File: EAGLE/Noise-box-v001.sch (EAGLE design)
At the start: 83 parts, among them J1 AVR_SPI_PROG_3X22X3_LOCK, J4 MICRO-SD_CARD_SOCKET, J5 HEADPHONE, J6 POWER_JACK, U1 ATMEGA328P_TQFP, U2 MIC5219 3.3V, U3 MCP73831, Y1 12.288MHz, Y2 8MHz

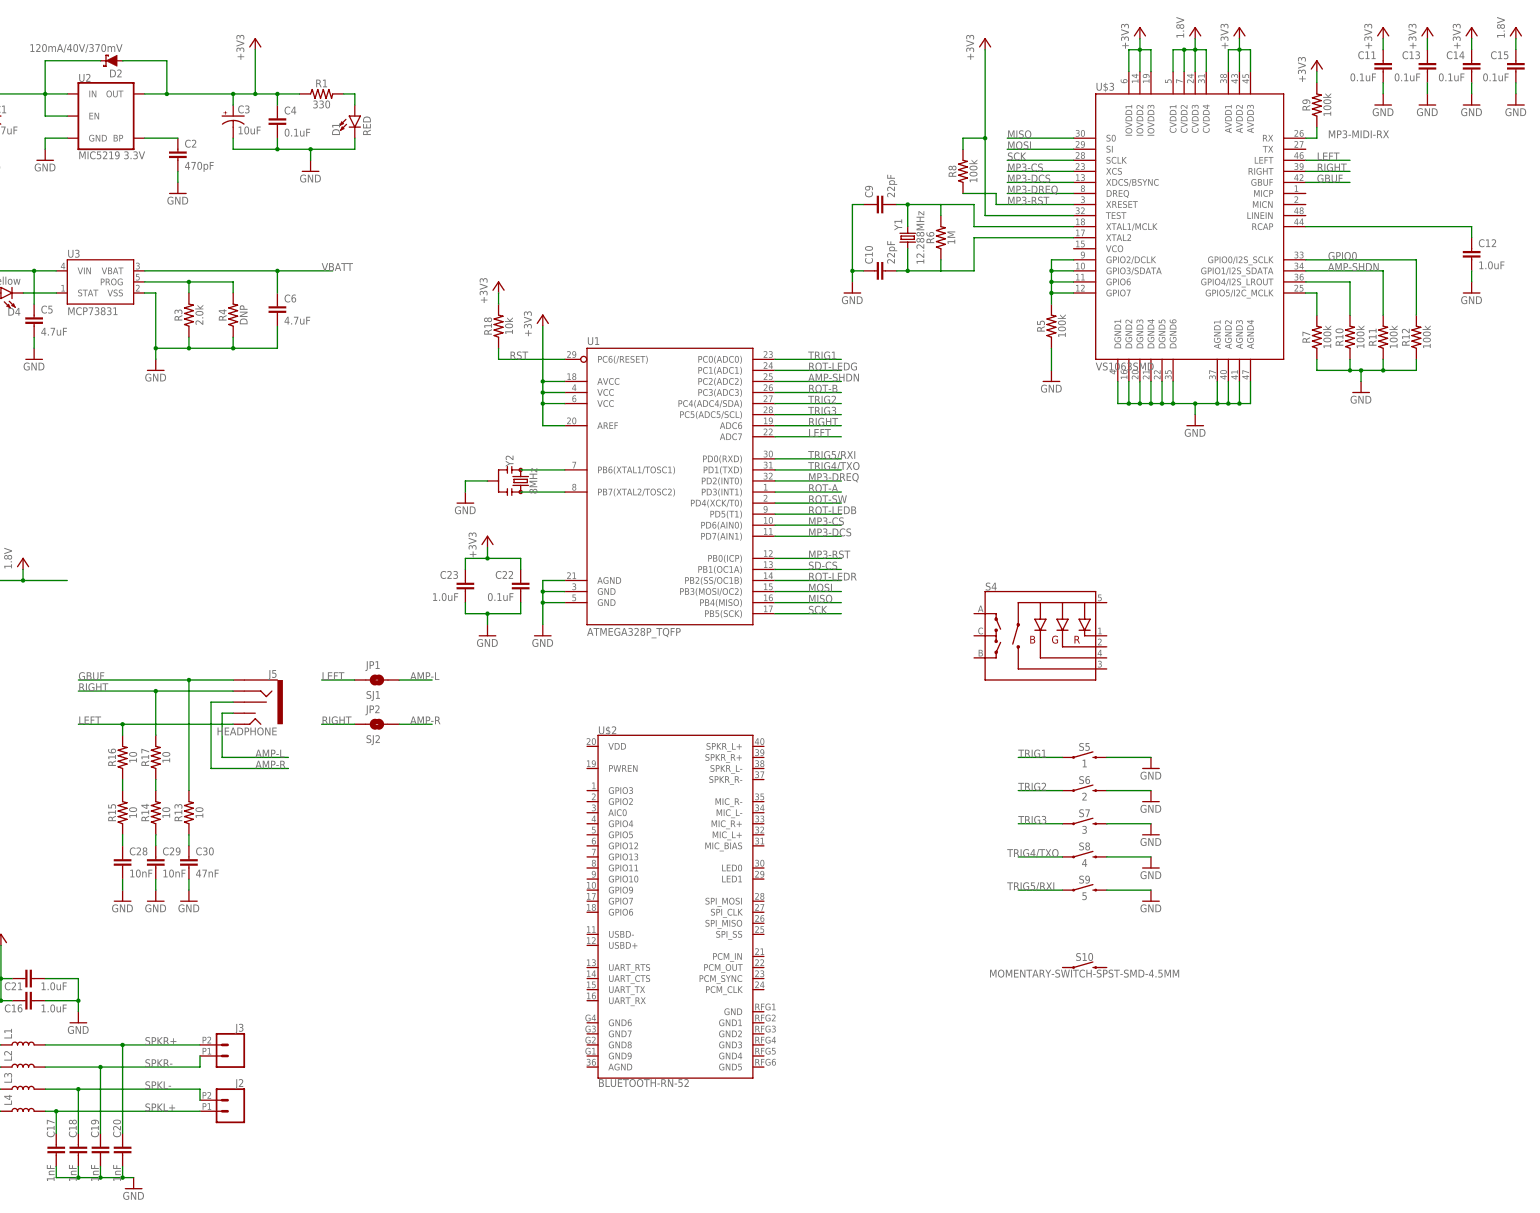
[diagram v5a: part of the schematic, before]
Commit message: More layout, buttons, debug header
Added a handful of buttons and a rotary switch to handle user inputs
such a track selection, volume knob, pause/play, etc. Added 5 pin debug
header for FTDI to USB adapter I have. Advanced the layout - nearly
complete.
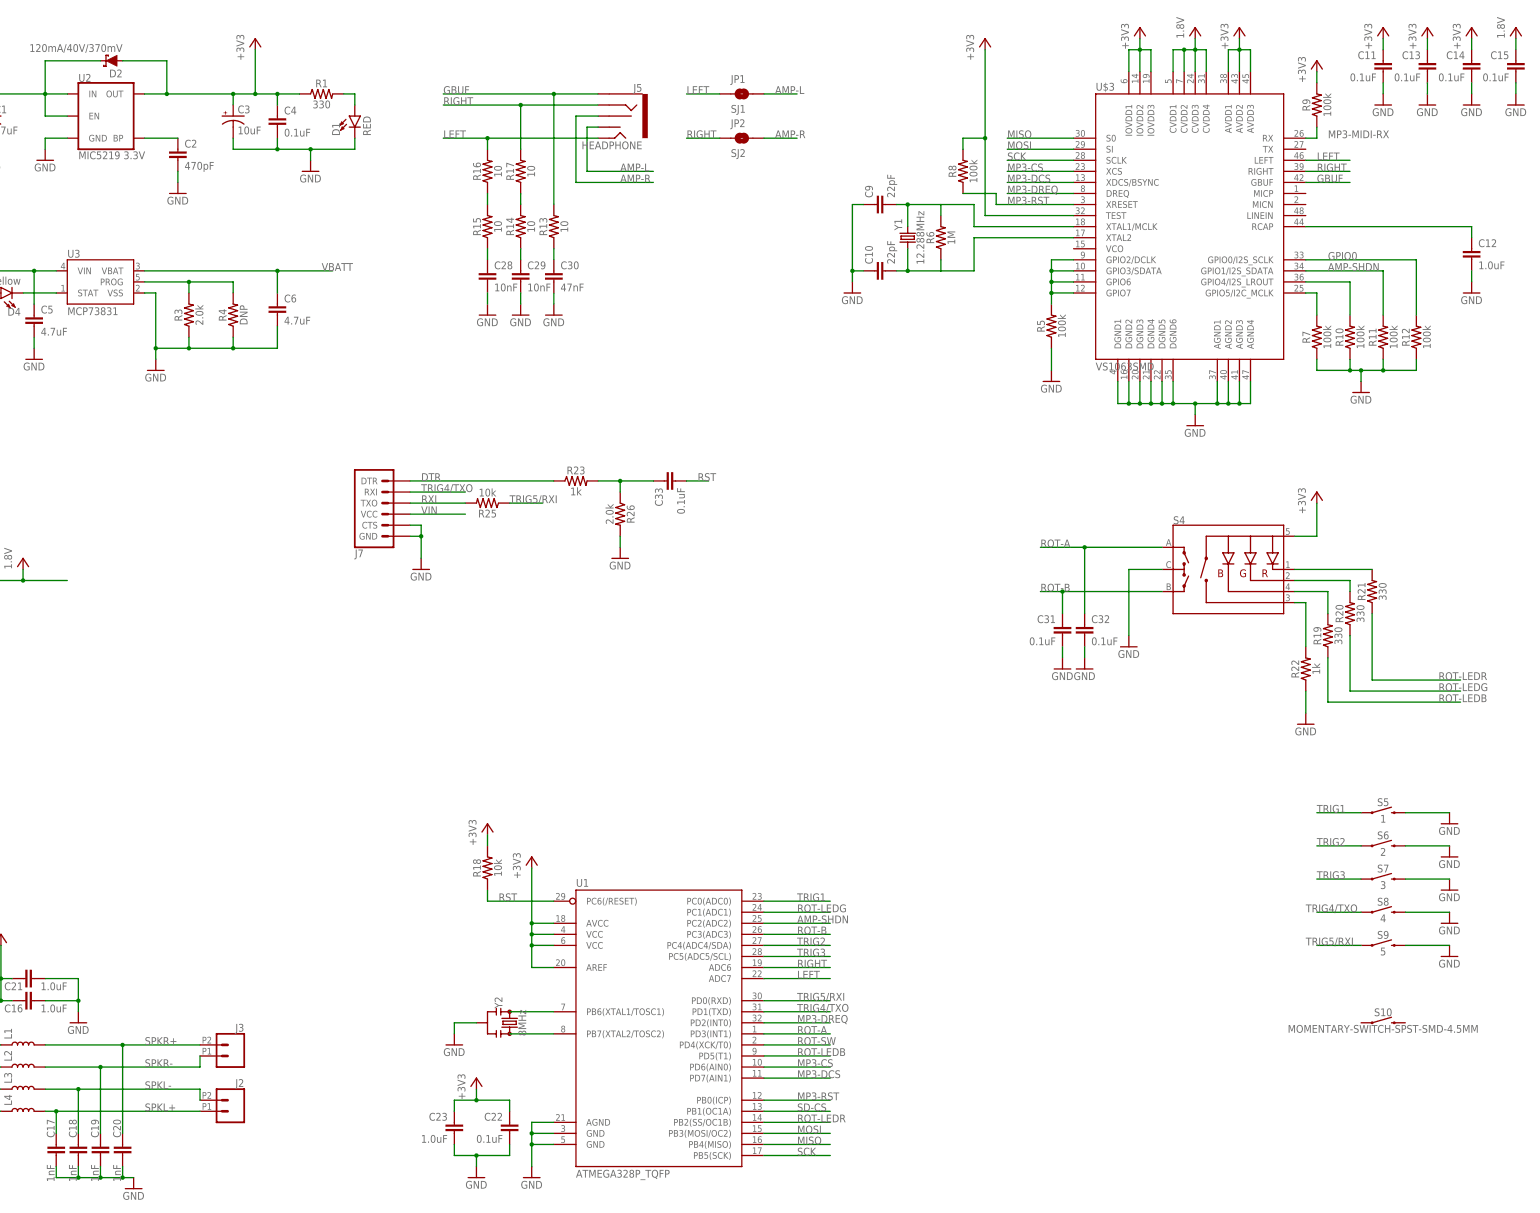
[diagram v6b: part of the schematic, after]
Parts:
- removed U$2: BLUETOOTH-RN-52, SparkFun-RF:BLUETOOTH-RN-52
- added C31, C32, C33: 0.1uF, SparkFun-Capacitors:0.1UF-0603-25V-5%
- added J7: (no value), SparkFun-Connectors:6_PIN_SERIAL_TARGETSILK
- added R19, R20, R21: 330, SparkFun-Resistors:330OHM-0603-1/10W-1%
- added R22, R23: 1k, SparkFun-Resistors:1KOHM-0603-1/10W-1%
- added R25: 10k, SparkFun-Resistors:10KOHM-0603-1/10W-1%
- added R26: 2.0k, SparkFun-Resistors:2.0KOHM-0603-1/10W-5%
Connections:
- new net DTR: J7.DTR, R23.1
- new net N$26: C33.1, R23.2, R26.1
- new net N$28: R22.2, S4.SW
- new net N$29: R19.2, S4.-B
- new net N$30: R20.2, S4.-G
- new net N$31: R21.2, S4.-R
- new net RXI: J7.TXO, R25.2
- net +3V3: now also S4.+
- net GND: now also C31.2, C32.2, J7.CTS, J7.GND, R22.1, R26.2, S4.C
- net ROT-A: now also C32.1, S4.A
- net ROT-B: now also C31.1, S4.B
- net ROT-LEDB: now also R19.1
- net ROT-LEDG: now also R20.1
- net ROT-LEDR: now also R21.1
- net RST: now also C33.2
- net TRIG4/TXO: now also J7.RXI
- net TRIG5/RXI: now also R25.1
- net VIN: now also J7.VCC
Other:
- moved on the sheet: C22, C23, C28, C29, C30, J5, JP1, JP2, R13, R14, R15, R16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

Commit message: Readme update
Added a bit of formatting. Continued the explanation of the project.
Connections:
- removed net N$28: R22.2, S4.SW
- net AMP-L: now also C27.1; no longer C26.1
- net GBUF: now also C26.1; no longer C27.1
- net ROT-SW: now also R22.2, S4.SW
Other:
- moved on the sheet: R22
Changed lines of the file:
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@@
 <instance part="GND37" gate="1" x="406.4" y="58.42"/>
 <instance part="GND38" gate="1" x="332.74" y="129.54"/>
-<instance part="GND39" gate="1" x="373.38" y="111.76"/>
+<instance part="GND39" gate="1" x="373.38" y="104.14"/>
 <instance part="+3V15" gate="G$1" x="375.92" y="165.1"/>
 <instance part="R19" gate="G$1" x="378.46" y="132.08" rot="R90"/>
 <instance part="R20" gate="G$1" x="383.54" y="137.16" rot="R90"/>
 <instance part="R21" gate="G$1" x="388.62" y="142.24" rot="R90"/>
-<instance part="R22" gate="G$1" x="373.38" y="124.46" rot="R90"/>
+<instance part="R22" gate="G$1" x="373.38" y="114.3" rot="R90"/>
 <instance part="C31" gate="G$1" x="317.5" y="132.08" rot="MR0"/>
 <instance part="C32" gate="G$1" x="322.58" y="132.08"/>
@@
 <pinref part="R22" gate="G$1" pin="1"/>
 <pinref part="GND39" gate="1" pin="GND"/>
-<wire x1="373.38" y1="119.38" x2="373.38" y2="114.3" width="0.1524" layer="91"/>
+<wire x1="373.38" y1="109.22" x2="373.38" y2="106.68" width="0.1524" layer="91"/>
 </segment>
 <segment>
@@
 </segment>
 <segment>
-<pinref part="C27" gate="G$1" pin="1"/>
-<wire x1="20.32" y1="33.02" x2="10.16" y2="33.02" width="0.1524" layer="91"/>
-<label x="5.08" y="33.02" size="1.778" layer="95"/>
-</segment>
-<segment>
 <pinref part="J5" gate="G$1" pin="SLEEVE"/>
 <wire x1="210.82" y1="256.54" x2="200.66" y2="256.54" width="0.1524" layer="91"/>
@@
 <wire x1="200.66" y1="231.14" x2="200.66" y2="256.54" width="0.1524" layer="91"/>
 <junction x="200.66" y="256.54"/>
+</segment>
+<segment>
+<pinref part="C26" gate="G$1" pin="1"/>
+<wire x1="20.32" y1="38.1" x2="10.16" y2="38.1" width="0.1524" layer="91"/>
+<label x="5.08" y="38.1" size="1.778" layer="95"/>
 </segment>
 </net>
@@
 <label x="256.54" y="38.1" size="1.778" layer="95"/>
 </segment>
+<segment>
+<pinref part="S4" gate="G$1" pin="SW"/>
+<wire x1="370.84" y1="139.7" x2="373.38" y2="139.7" width="0.1524" layer="91"/>
+<wire x1="373.38" y1="139.7" x2="373.38" y2="119.38" width="0.1524" layer="91"/>
+<pinref part="R22" gate="G$1" pin="2"/>
+<label x="373.38" y="124.46" size="1.778" layer="95" rot="R90"/>
+</segment>
 </net>
 <net name="ROT-A" class="0">
@@
 <net name="AMP-L" class="0">
 <segment>
-<pinref part="C26" gate="G$1" pin="1"/>
-<wire x1="20.32" y1="38.1" x2="10.16" y2="38.1" width="0.1524" layer="91"/>
-<label x="5.08" y="38.1" size="1.778" layer="95"/>
-</segment>
-<segment>
 <pinref part="JP1" gate="G$1" pin="2"/>
 <wire x1="248.92" y1="256.54" x2="256.54" y2="256.54" width="0.1524" layer="91"/>
@@
 <wire x1="208.28" y1="238.76" x2="223.52" y2="238.76" width="0.1524" layer="91"/>
 <label x="215.9" y="238.76" size="1.778" layer="95"/>
+</segment>
+<segment>
+<pinref part="C27" gate="G$1" pin="1"/>
+<wire x1="20.32" y1="33.02" x2="10.16" y2="33.02" width="0.1524" layer="91"/>
+<label x="5.08" y="33.02" size="1.778" layer="95"/>
 </segment>
 </net>
@@
 </segment>
 </net>
-<net name="N$28" class="0">
-<segment>
-<pinref part="S4" gate="G$1" pin="SW"/>
-<wire x1="370.84" y1="139.7" x2="373.38" y2="139.7" width="0.1524" layer="91"/>
-<wire x1="373.38" y1="139.7" x2="373.38" y2="129.54" width="0.1524" layer="91"/>
-<pinref part="R22" gate="G$1" pin="2"/>
-</segment>
-</net>

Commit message: Layout, CAM, BoM, Datasheets
Finished layout, generated CAM files for manufacturing, generated BoM.
Added several datasheets for reference
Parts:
- removed S10: MOMENTARY-SWITCH-SPST-SMD-4.5MM, SparkFun-Switches:MOMENTARY-SWITCH-SPST-SMD-4.5MM
- BT2: value (none) -> 18650
- J2: value (none) -> LEFT
- J3: value (none) -> RIGHT
- J7: value (none) -> FTDI
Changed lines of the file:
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@@
 <parts>
 <part name="U1" library="SparkFun-IC-Microcontroller" deviceset="ATMEGA328P_TQFP" device="" value="ATMEGA328P_TQFP"/>
-<part name="FRAME1" library="frames" deviceset="FRAME_B_L" device=""/>
+<part name="FRAME1" library="frames" deviceset="FRAME_B_L" device="" value="Noise Box v01"/>
 <part name="+3V1" library="supply1" deviceset="+3V3" device=""/>
 <part name="GND1" library="supply1" deviceset="GND" device=""/>
@@
 <part name="GND29" library="supply1" deviceset="GND" device=""/>
 <part name="GND30" library="supply1" deviceset="GND" device=""/>
-<part name="J2" library="SparkFun-Connectors" deviceset="CONN_02" device="2.54MM_SCREWTERM"/>
-<part name="J3" library="SparkFun-Connectors" deviceset="CONN_02" device="2.54MM_SCREWTERM"/>
+<part name="J2" library="SparkFun-Connectors" deviceset="CONN_02" device="2.54MM_SCREWTERM" value="LEFT"/>
+<part name="J3" library="SparkFun-Connectors" deviceset="CONN_02" device="2.54MM_SCREWTERM" value="RIGHT"/>
 <part name="R2" library="SparkFun-Resistors" deviceset="470OHM" device="-0603-1/10W-1%" value="470"/>
-<part name="BT2" library="MAK" deviceset="BATTERY" device="-1043P"/>
+<part name="BT2" library="MAK" deviceset="BATTERY" device="-1043P" value="18650"/>
 <part name="GND8" library="supply1" deviceset="GND" device=""/>
 <part name="GND2" library="supply1" deviceset="GND" device=""/>
@@
 <part name="S8" library="SparkFun-Switches" deviceset="MOMENTARY-SWITCH-SPST" device="-SMD-4.5MM" value="4"/>
 <part name="S9" library="SparkFun-Switches" deviceset="MOMENTARY-SWITCH-SPST" device="-SMD-4.5MM" value="5"/>
-<part name="S10" library="SparkFun-Switches" deviceset="MOMENTARY-SWITCH-SPST" device="-SMD-4.5MM"/>
 <part name="GND33" library="supply1" deviceset="GND" device=""/>
 <part name="GND34" library="supply1" deviceset="GND" device=""/>
@@
 <part name="GND40" library="supply1" deviceset="GND" device=""/>
 <part name="GND41" library="supply1" deviceset="GND" device=""/>
-<part name="J7" library="SparkFun-Connectors" deviceset="6_PIN_SERIAL_TARGET" device="SILK"/>
+<part name="J7" library="SparkFun-Connectors" deviceset="6_PIN_SERIAL_TARGET" device="SILK" value="FTDI"/>
 <part name="GND42" library="supply1" deviceset="GND" device=""/>
 <part name="R23" library="SparkFun-Resistors" deviceset="1KOHM" device="-0603-1/10W-1%" value="1k"/>
@@
 <instance part="S8" gate="G$1" x="391.16" y="68.58"/>
 <instance part="S9" gate="G$1" x="391.16" y="60.96"/>
-<instance part="S10" gate="G$1" x="391.16" y="43.18"/>
 <instance part="GND33" gate="1" x="406.4" y="81.28"/>
 <instance part="GND34" gate="1" x="406.4" y="88.9"/>
@@
 <wire x1="297.18" y1="226.06" x2="297.18" y2="231.14" width="0.1524" layer="91"/>
 <wire x1="297.18" y1="231.14" x2="289.56" y2="231.14" width="0.1524" layer="91"/>
+<junction x="289.56" y="231.14"/>
 </segment>
 </net>
@@
 <wire x1="297.18" y1="223.52" x2="297.18" y2="215.9" width="0.1524" layer="91"/>
 <wire x1="297.18" y1="215.9" x2="289.56" y2="215.9" width="0.1524" layer="91"/>
+<junction x="289.56" y="215.9"/>
 </segment>
 </net>
@@
 </sheet>
 </sheets>
+<errors>
+</errors>
 </schematic>
 </drawing>
